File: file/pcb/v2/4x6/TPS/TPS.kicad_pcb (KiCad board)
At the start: 2 copper layers, 164 x 76.2 mm, 95 parts, among them J1 I2C, J2 FFC-0.5mm, 12p, J3 FFC-0.5mm, 12p, J4 PH2.0-2pin, J5 FFC-0.5mm, 6p, J6 FFC-0.5mm, 6p, K1 SW_Push, K10 SW_Push, K11 SW_Push, K12 SW_Push, K13 SW_Push, K14 SW_Push, K15 SW_Push, K16 SW_Push, K17 SW_Push, K18 SW_Push, K19 SW_Push, K2 SW_Push, K20 SW_Push, K21 SW_Push, K22 SW_Push, K23 SW_Push, K24 SW_Push, K25 EC-11, K3 SW_Push, K4 SW_Push, K5 SW_Push, K6 SW_Push, K7 SW_Push, K8 SW_Push, K9 SW_Push, SW1 SW_Push, SW2 MSKT-12D14, SW3 MSKT-12D14, T1 AudioJack4, U1 MCU_ProMicro_13p

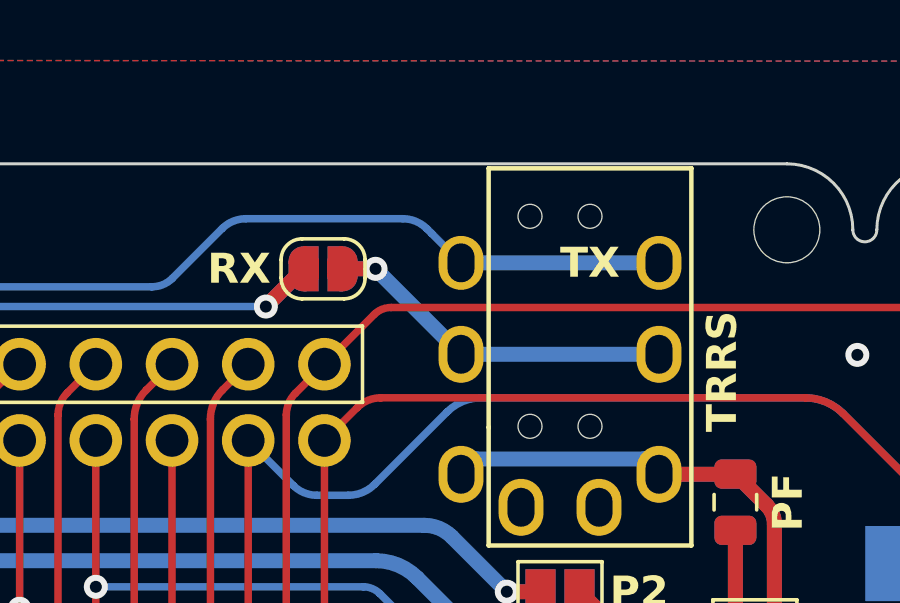
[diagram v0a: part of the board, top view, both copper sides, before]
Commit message: fix TRRS TX/RX pins
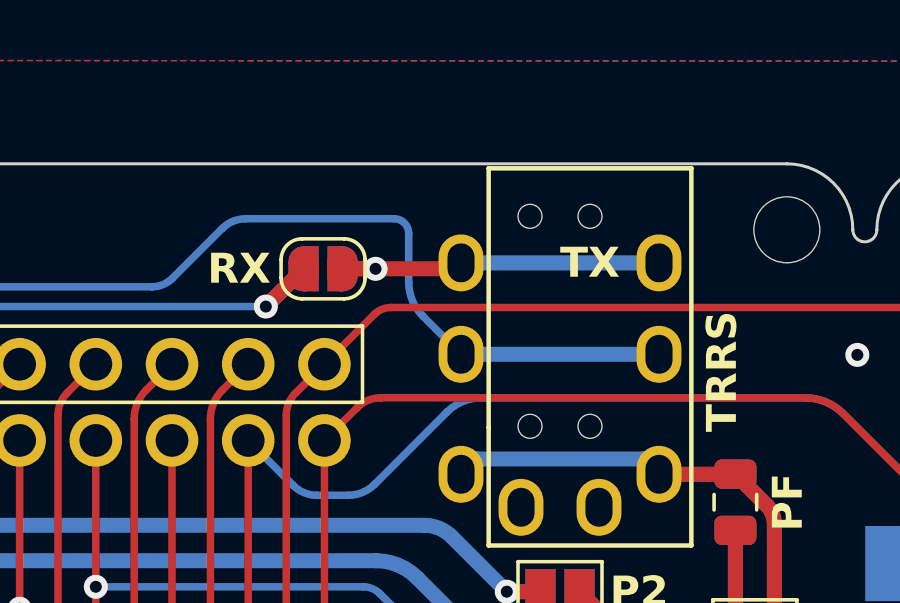
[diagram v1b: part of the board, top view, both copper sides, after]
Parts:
- removed T1: AudioJack4, DreaM117er-keebLibrary:TRRS-PJ-320A, dual side x2
- added J9: AudioJack4, DreaM117er-keebLibrary:TRRS-PJ-320A, dual side x2, F.Cu at (78.2, 29.1)
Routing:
- net TX: track 60.2 -> 62.9 mm
- net Net-(JP13-B): track 12.8 -> 11.7 mm

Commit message: fix main PCB file UI
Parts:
- J9: footprint DreaM117er-keebLibrary:TRRS-PJ-320A, dual side x2 -> DreaM117er-keebLibrary:TRRS-PJ-320A, dual side x2_3rd
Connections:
- H10 pad : GND -> (no net)
- H11 pad : GND -> (no net)
- H8 pad : GND -> (no net)
- H9 pad : GND -> (no net)
- SW2 pad 3: unconnected-(SW2-C-Pad3) -> N/A1
- SW3 pad 3: unconnected-(SW3-C-Pad3) -> N/A2
- U1 pad 9: unconnected-(U1-5/PC6-Pad9)_1 -> row4
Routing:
- net unconnected-(U1-5/PC6-Pad9)_1: track 18.7 -> 0.00 mm
- net row4: track 0.00 -> 18.7 mm
- net unconnected-(SW2-C-Pad3): track 3.71 -> 0.00 mm, vias 1 -> 0
- net N/A1: track 0.00 -> 3.71 mm, vias 0 -> 1
- net unconnected-(SW3-C-Pad3): track 3.71 -> 0.00 mm, vias 1 -> 0
- net N/A2: track 0.00 -> 3.71 mm, vias 0 -> 1
